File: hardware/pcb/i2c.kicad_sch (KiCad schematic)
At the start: 25 parts, among them Q1 CSD13380F3, U10 AS7341-DLGM, U11 TMP117AIDRVR, U12 MLX90632SLD-DCB-100-SP, U13 BME280, U14 LSM6DSV80XTR, U20 TMP117AIDRVR, U9 PCA9306DCUR

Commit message: Fix the review's datasheet errors without changing respiration or the GDTs.
Replace the MCP73831 with a BQ25170 so a flat cell still charges from USB, add the missing series protection and ESP32/CP2102 passives, and withdraw the claim that respiration still works with 51 kΩ in the loop.

Co-authored-by: Riyu-D1 <Riyu-D1@users.noreply.github.com>
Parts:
- added R66: 301k, Resistor_SMD:R_0402_1005Metric, symbol vitalq:R
- R18: value 200 -> 200k
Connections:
- net +1V8: now also R66.1
- net GND: now also R66.2

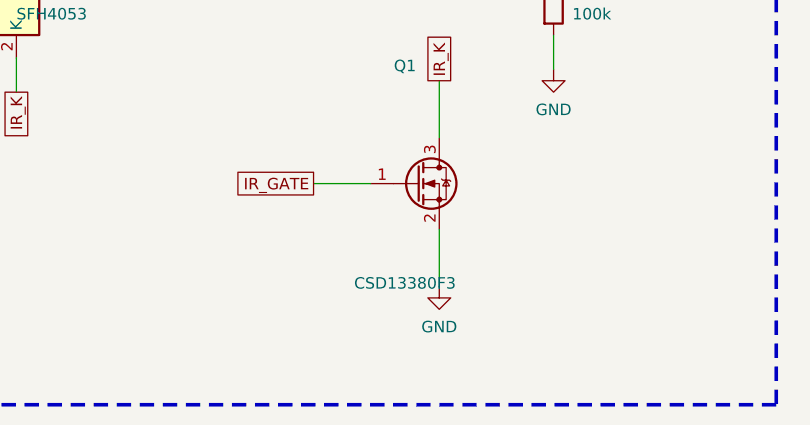
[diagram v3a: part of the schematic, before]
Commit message: Prepare hw_v1 for prefab review without claiming the route is finished.
Add the gauge TDFN, USB ESD, sense links, test access, and JLC BOM fields, and keep the partial Freerouting result with the remaining open nets listed.

Co-authored-by: Riyu-D1 <Riyu-D1@users.noreply.github.com>
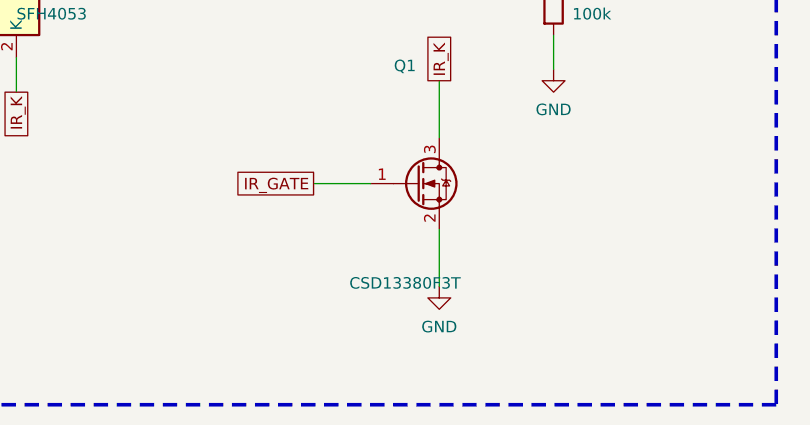
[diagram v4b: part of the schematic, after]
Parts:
- Q1: value CSD13380F3 -> CSD13380F3T
- U11, U20: footprint snap:SON65P200X200X80-7N -> vitalq:TMP117_DRV_NOPASTE
